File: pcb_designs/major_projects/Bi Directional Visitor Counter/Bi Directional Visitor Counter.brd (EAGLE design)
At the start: 6.9 x 7 mm, 27 parts, among them IC1 AT89S51, IC2 7805TV

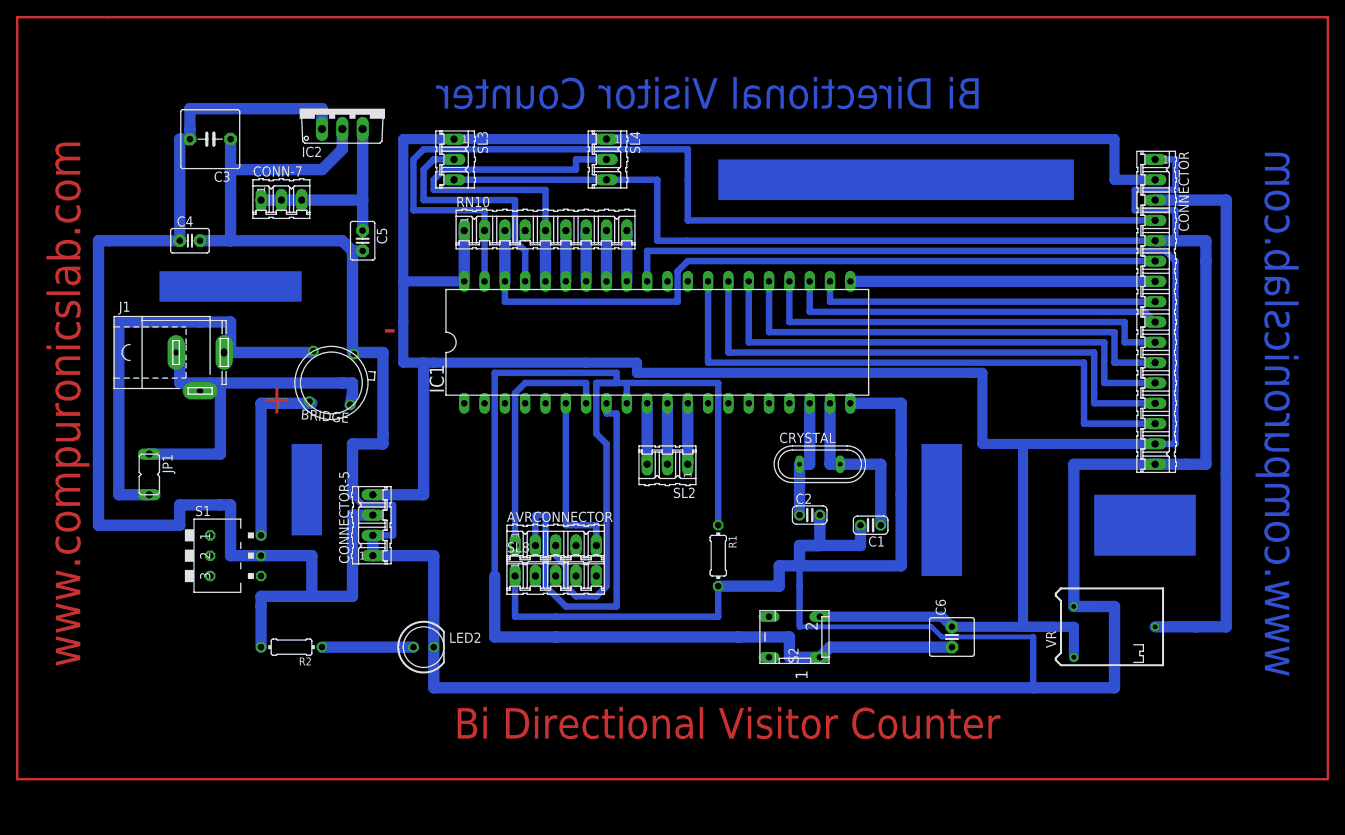
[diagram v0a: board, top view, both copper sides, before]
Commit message: 
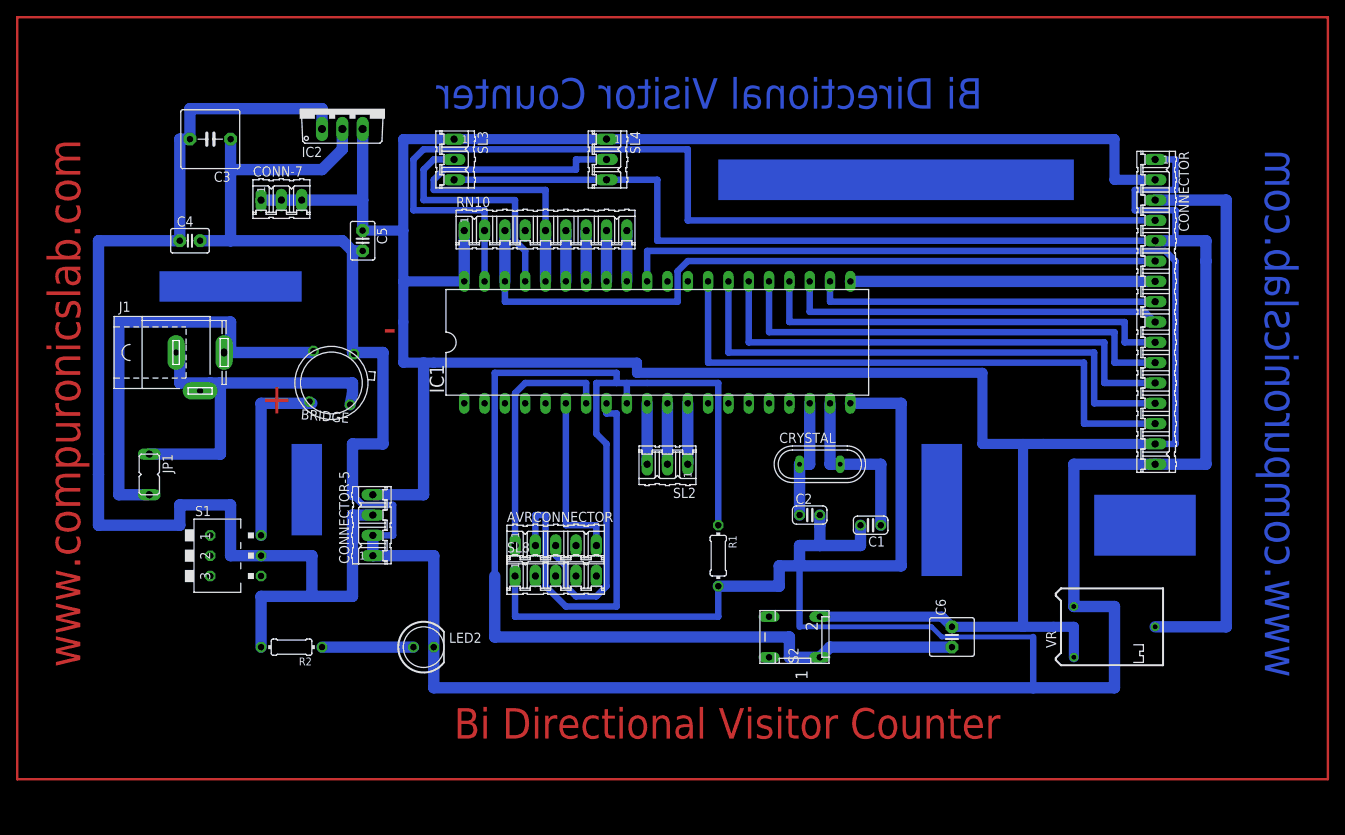
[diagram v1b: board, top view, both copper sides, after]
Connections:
- removed net N$8: C6.2, CONNECTOR-5.4, CONNECTOR.15, CONNECTOR.2, IC1.31, IC1.40, RN10.1, S2.2, SL3.1, SL4.1, VR.1
- net N$39: now also C6.2, CONNECTOR-5.4, CONNECTOR.15, CONNECTOR.2, IC1.31, IC1.40, RN10.1, S2.2, SL3.1, SL4.1, VR.1
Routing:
- net N$8: track 440.5 -> 0.00 mm
- net N$39: track 25.4 -> 457.0 mm
- net N$41: track 593.7 -> 569.3 mm
- net N$4: track 158.7 -> 153.7 mm
- net N$14: track 188.1 -> 185.5 mm
- net N$16: track 52.8 -> 51.5 mm
- net N$5: track 55.2 -> 54.4 mm
